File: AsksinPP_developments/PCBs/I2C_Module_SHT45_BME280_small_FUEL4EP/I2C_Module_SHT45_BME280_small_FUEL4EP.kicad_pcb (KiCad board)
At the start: 2 copper layers, 14.1 x 17 mm, 13 parts, among them J1 Conn_01x04, U1 BME280, U2 SHT45-AD1B-R2

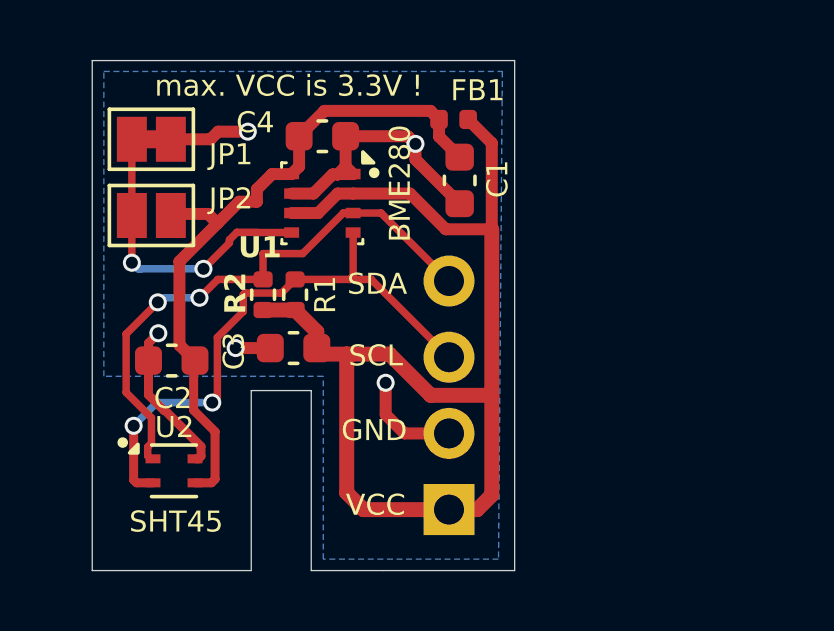
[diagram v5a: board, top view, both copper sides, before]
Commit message: added PCBs/I2C_Module_BME680_small_FUEL4EP; corrected JLCPCB miinimum spacing in DRC rules
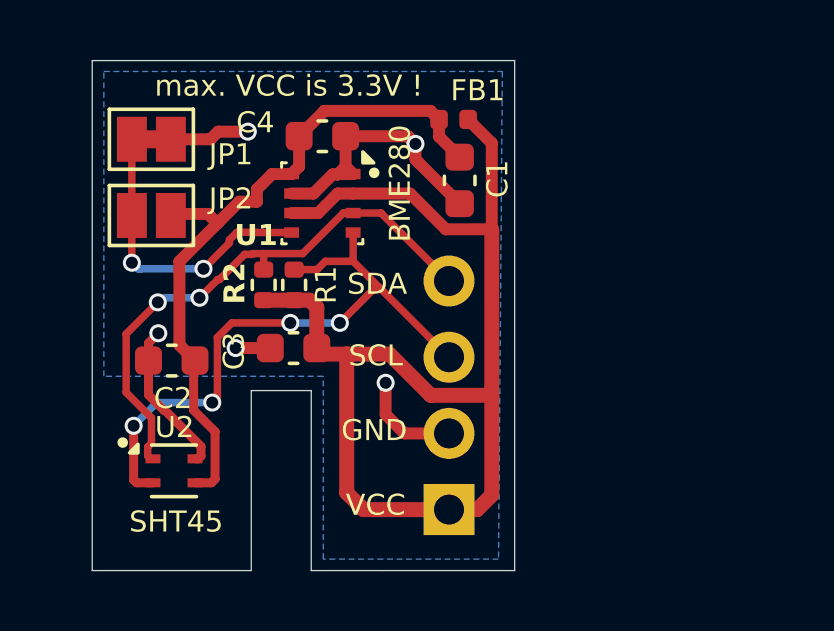
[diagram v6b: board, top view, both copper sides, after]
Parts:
- moved R2 0.33 mm to (6.73, -9.52)
- moved R1 0.33 mm to (5.71, -9.52)
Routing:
- net /SCL: track 19.2 -> 21.3 mm, vias 2 -> 4
- net VCC: track 39.0 -> 39.6 mm
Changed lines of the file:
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@@
 		(tags "lga land grid array")
 		(property "Reference" "U1"
-			(at 1.4732 2.0828 0)
+			(at 1.0668 2.2098 0)
 			(layer "F.SilkS")
 			(effects
@@
 	(footprint "Resistor_SMD:R_0402_1005Metric"
 		(layer "F.Cu")
-		(at 5.6944 -9.1948 -90)
+		(at 5.715 -9.523 -90)
 		(descr "Resistor SMD 0402 (1005 Metric), square (rectangular) end terminal, IPC_7351 nominal, (Body size source: IPC-SM-782 page 72, https://www.pcb-3d.com/wordpress/wp-content/uploads/ipc-sm-782a_amendment_1_and_2.pdf), generated with kicad-footprint-generator")
 		(tags "resistor")
@@
 	(footprint "Resistor_SMD:R_0402_1005Metric"
 		(layer "F.Cu")
-		(at 6.7612 -9.1948 -90)
+		(at 6.731 -9.523 -90)
 		(descr "Resistor SMD 0402 (1005 Metric), square (rectangular) end terminal, IPC_7351 nominal, (Body size source: IPC-SM-782 page 72, https://www.pcb-3d.com/wordpress/wp-content/uploads/ipc-sm-782a_amendment_1_and_2.pdf), generated with kicad-footprint-generator")
 		(tags "resistor")
@@
 	)
 	(segment
-		(start 7.4854 -7.4168)
-		(end 7.4854 -7.9606)
+		(start 6.731 -9.013)
+		(end 5.715 -9.013)
 		(width 0.5)
 		(layer "F.Cu")
@@
 	)
 	(segment
-		(start 7.4854 -7.9606)
-		(end 6.7612 -8.6848)
-		(width 0.5)
+		(start 11.785343 -11.3756)
+		(end 13.318 -11.3756)
+		(width 0.4)
 		(layer "F.Cu")
 		(net 1)
 	)
 	(segment
-		(start 11.785343 -11.3756)
-		(end 13.318 -11.3756)
-		(width 0.4)
+		(start 7.4854 -7.4168)
+		(end 7.4854 -8.7706)
+		(width 0.5)
 		(layer "F.Cu")
 		(net 1)
 	)
 	(segment
-		(start 6.7612 -8.6848)
-		(end 5.6944 -8.6848)
+		(start 7.4854 -8.7706)
+		(end 7.243 -9.013)
 		(width 0.5)
 		(layer "F.Cu")
@@
 	)
 	(segment
+		(start 7.243 -9.013)
+		(end 6.731 -9.013)
+		(width 0.5)
+		(layer "F.Cu")
+		(net 1)
+	)
+	(segment
 		(start 13.2708 -5.842)
 		(end 13.318 -5.7948)
@@
 	)
 	(segment
-		(start 6.3062 -9.2498)
-		(end 6.7612 -9.7048)
-		(width 0.25)
-		(layer "F.Cu")
-		(net 3)
-	)
-	(segment
-		(start 8.6958 -11.2678)
-		(end 8.6958 -9.8134)
-		(width 0.25)
-		(layer "F.Cu")
-		(net 3)
-	)
-	(segment
-		(start 11.892 -7.112)
-		(end 9.3102 -9.6938)
-		(width 0.25)
-		(layer "F.Cu")
-		(net 3)
-	)
-	(segment
-		(start 5.089 -9.2498)
-		(end 6.3062 -9.2498)
+		(start 4.653 -8.255)
+		(end 6.604 -8.255)
 		(width 0.25)
 		(layer "F.Cu")
@@
 	)
 	(segment
-		(start 8.5872 -9.7048)
-		(end 9.2992 -9.7048)
+		(start 7.493 -10.033)
+		(end 6.731 -10.033)
 		(width 0.25)
 		(layer "F.Cu")
@@
 	)
 	(segment
-		(start 5.034 -8.636)
-		(end 5.034 -9.1948)
+		(start 4.17 -7.772)
+		(end 4.653 -8.255)
 		(width 0.25)
 		(layer "F.Cu")
@@
 	)
 	(segment
-		(start 9.2992 -9.7048)
-		(end 9.3102 -9.6938)
+		(start 9.4385 -9.4385)
+		(end 9.5655 -9.4385)
 		(width 0.25)
 		(layer "F.Cu")
@@
 	)
 	(segment
-		(start 8.6958 -9.8134)
-		(end 8.5872 -9.7048)
+		(start 9.5655 -9.4385)
+		(end 8.6958 -10.3082)
 		(width 0.25)
 		(layer "F.Cu")
@@
 	)
 	(segment
-		(start 6.7612 -9.7048)
-		(end 8.5872 -9.7048)
+		(start 8.255 -8.255)
+		(end 9.4385 -9.4385)
 		(width 0.25)
 		(layer "F.Cu")
@@
 	)
 	(segment
-		(start 4.17 -7.772)
-		(end 5.034 -8.636)
+		(start 8.6958 -10.3082)
+		(end 7.7682 -10.3082)
 		(width 0.25)
 		(layer "F.Cu")
@@
 	)
 	(segment
-		(start 5.034 -9.1948)
-		(end 5.089 -9.2498)
+		(start 7.7682 -10.3082)
+		(end 7.493 -10.033)
 		(width 0.25)
 		(layer "F.Cu")
@@
 	)
 	(segment
+		(start 8.6958 -10.3082)
+		(end 8.6958 -11.2678)
+		(width 0.25)
+		(layer "F.Cu")
+		(net 3)
+	)
+	(segment
 		(start 4.17 -7.772)
 		(end 4.17 -5.77)
@@
 		(net 3)
 	)
+	(segment
+		(start 11.892 -7.112)
+		(end 9.5655 -9.4385)
+		(width 0.25)
+		(layer "F.Cu")
+		(net 3)
+	)
+	(via
+		(at 6.604 -8.255)
+		(size 0.6)
+		(drill 0.4)
+		(layers "F.Cu" "B.Cu")
+		(net 3)
+	)
 	(via
 		(at 1.38 -4.826)
@@
 	)
 	(via
+		(at 8.255 -8.255)
+		(size 0.6)
+		(drill 0.4)
+		(layers "F.Cu" "B.Cu")
+		(net 3)
+	)
+	(via
 		(at 4 -5.6)
 		(size 0.6)
@@
 	)
 	(segment
+		(start 6.604 -8.255)
+		(end 8.255 -8.255)
+		(width 0.25)
+		(layer "B.Cu")
+		(net 3)
+	)
+	(segment
 		(start 9.6262 -11.9178)
 		(end 8.6958 -11.9178)
@@
 	)
 	(segment
+		(start 5.6944 -10.5664)
+		(end 5.715 -10.5458)
+		(width 0.25)
+		(layer "F.Cu")
+		(net 4)
+	)
+	(segment
 		(start 11.892 -9.652)
 		(end 9.6262 -11.9178)
@@
 	)
 	(segment
+		(start 5.08 -10.541)
+		(end 5.334 -10.541)
+		(width 0.25)
+		(layer "F.Cu")
+		(net 4)
+	)
+	(segment
 		(start 5.6944 -10.5664)
 		(end 7.0152 -10.5664)
@@
 	)
 	(segment
-		(start 1.85 -3.823222)
-		(end 1.948222 -3.725)
+		(start 5.715 -10.5458)
+		(end 5.715 -10.033)
 		(width 0.25)
 		(layer "F.Cu")
@@
 	)
 	(segment
-		(start 5.6944 -9.7048)
-		(end 4.187592 -9.7048)
+		(start 4.187592 -9.7048)
+		(end 4.2438 -9.7048)
 		(width 0.25)
 		(layer "F.Cu")
@@
 	)
 	(segment
-		(start 1.9745 -5.0915)
-		(end 1.9745 -4.251278)
+		(start 1.85 -3.823222)
+		(end 1.948222 -3.725)
 		(width 0.25)
 		(layer "F.Cu")
@@
 	)
 	(segment
-		(start 5.6944 -9.7048)
-		(end 5.6944 -10.5664)
+		(start 1.9745 -5.0915)
+		(end 1.9745 -4.251278)
 		(width 0.25)
 		(layer "F.Cu")
@@
 	)
 	(segment
+		(start 5.334 -10.541)
+		(end 5.3594 -10.5664)
+		(width 0.25)
+		(layer "F.Cu")
+		(net 4)
+	)
+	(segment
 		(start 8.6958 -11.9178)
 		(end 8.3666 -11.9178)
@@
 	)
 	(segment
+		(start 4.2438 -9.7048)
+		(end 5.08 -10.541)
+		(width 0.25)
+		(layer "F.Cu")
+		(net 4)
+	)
+	(segment
 		(start 1.9745 -4.251278)
 		(end 1.85 -4.126778)
@@
 		(width 0.25)
 		(layer "F.Cu")
+		(net 4)
+	)
+	(segment
+		(start 5.3594 -10.5664)
+		(end 5.6944 -10.5664)
+		(width 0.25)
+		(layer "F.Cu")

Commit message: PCBs: updated some JLCPCB manufacturing data after trial-order
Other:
- board text added: "JLCJLCJLCJLC"
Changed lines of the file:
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@@
 		(sheetfile "I2C_Module_SHT45_BME280_small_FUEL4EP.kicad_sch")
 		(zone_connect 1)
-		(attr exclude_from_pos_files)
+		(attr exclude_from_pos_files exclude_from_bom)
 		(fp_line
 			(start -1.4 -1)
@@
 		(sheetfile "I2C_Module_SHT45_BME280_small_FUEL4EP.kicad_sch")
 		(zone_connect 1)
-		(attr exclude_from_pos_files)
+		(attr exclude_from_pos_files exclude_from_bom)
 		(net_tie_pad_groups "1, 2")
 		(fp_poly
@@
 		(sheetname "Stammblatt")
 		(sheetfile "I2C_Module_SHT45_BME280_small_FUEL4EP.kicad_sch")
-		(attr through_hole exclude_from_pos_files)
+		(attr through_hole exclude_from_pos_files exclude_from_bom)
 		(fp_line
 			(start -1.33 -8.95)
@@
 			(size 1.7 1.7)
 			(drill 1)
-			(layers "*.Cu" "*.Mask")
+			(layers "*.Cu" "*.Mask" "In1.Cu" "In2.Cu" "In3.Cu" "In4.Cu" "In5.Cu" "In6.Cu"
+				"In7.Cu" "In8.Cu" "In9.Cu" "In10.Cu" "In11.Cu" "In12.Cu" "In13.Cu" "In14.Cu"
+				"In15.Cu" "In16.Cu" "In17.Cu" "In18.Cu" "In19.Cu" "In20.Cu" "In21.Cu"
+				"In22.Cu" "In23.Cu" "In24.Cu" "In25.Cu" "In26.Cu" "In27.Cu" "In28.Cu"
+				"In29.Cu" "In30.Cu"
+			)
 			(remove_unused_layers no)
 			(net 1 "VCC")
@@
 			(size 1.7 1.7)
 			(drill 1)
-			(layers "*.Cu" "*.Mask")
+			(layers "*.Cu" "*.Mask" "In1.Cu" "In2.Cu" "In3.Cu" "In4.Cu" "In5.Cu" "In6.Cu"
+				"In7.Cu" "In8.Cu" "In9.Cu" "In10.Cu" "In11.Cu" "In12.Cu" "In13.Cu" "In14.Cu"
+				"In15.Cu" "In16.Cu" "In17.Cu" "In18.Cu" "In19.Cu" "In20.Cu" "In21.Cu"
+				"In22.Cu" "In23.Cu" "In24.Cu" "In25.Cu" "In26.Cu" "In27.Cu" "In28.Cu"
+				"In29.Cu" "In30.Cu"
+			)
 			(remove_unused_layers no)
 			(net 2 "GND")
@@
 			(size 1.7 1.7)
 			(drill 1)
-			(layers "*.Cu" "*.Mask")
+			(layers "*.Cu" "*.Mask" "In1.Cu" "In2.Cu" "In3.Cu" "In4.Cu" "In5.Cu" "In6.Cu"
+				"In7.Cu" "In8.Cu" "In9.Cu" "In10.Cu" "In11.Cu" "In12.Cu" "In13.Cu" "In14.Cu"
+				"In15.Cu" "In16.Cu" "In17.Cu" "In18.Cu" "In19.Cu" "In20.Cu" "In21.Cu"
+				"In22.Cu" "In23.Cu" "In24.Cu" "In25.Cu" "In26.Cu" "In27.Cu" "In28.Cu"
+				"In29.Cu" "In30.Cu"
+			)
 			(remove_unused_layers no)
 			(net 3 "/SCL")
@@
 			(size 1.7 1.7)
 			(drill 1)
-			(layers "*.Cu" "*.Mask")
+			(layers "*.Cu" "*.Mask" "In1.Cu" "In2.Cu" "In3.Cu" "In4.Cu" "In5.Cu" "In6.Cu"
+				"In7.Cu" "In8.Cu" "In9.Cu" "In10.Cu" "In11.Cu" "In12.Cu" "In13.Cu" "In14.Cu"
+				"In15.Cu" "In16.Cu" "In17.Cu" "In18.Cu" "In19.Cu" "In20.Cu" "In21.Cu"
+				"In22.Cu" "In23.Cu" "In24.Cu" "In25.Cu" "In26.Cu" "In27.Cu" "In28.Cu"
+				"In29.Cu" "In30.Cu"
+			)
 			(remove_unused_layers no)
 			(net 4 "/SDA")
@@
 		(sheetname "Stammblatt")
 		(sheetfile "I2C_Module_SHT45_BME280_small_FUEL4EP.kicad_sch")
-		(attr through_hole)
+		(attr through_hole exclude_from_pos_files exclude_from_bom)
 		(fp_poly
 			(pts
@@
 		)
 	)
+	(gr_text "JLCJLCJLCJLC"
+		(at 8.128 -0.889 -90)
+		(layer "B.SilkS")
+		(effects
+			(font
+				(size 0.8128 0.8128)
+				(thickness 0.1524)
+				(bold yes)
+			)
+			(justify left bottom mirror)
+		)
+	)

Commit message: PCB updates
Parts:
- U2: footprint Sensor_Humidity:Sensirion_DFN-4_1.5x1.5mm_P0.8mm_SHT4x_NoCentralPad -> FUEL4EP:Sensirion_DFN-4_1.5x1.5mm_P0.8mm_SHT4x_NoCentralPad
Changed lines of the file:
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@@
+			)
+		)
+		(property "Sim.Enable" ""
+			(at 0 0 -90)
+			(unlocked yes)
+			(layer "F.Fab")
+			(hide yes)
+			(effects
+				(font
+					(size 1 1)
+					(thickness 0.15)
+				)
 			)
 		)
@@
 			)
 		)
+		(property "Sim.Enable" ""
+			(at 0 0 180)
+			(unlocked yes)
+			(layer "F.Fab")
+			(hide yes)
+			(effects
+				(font
+					(size 1 1)
+					(thickness 0.15)
+				)
+			)
+		)
 		(property ki_fp_filters "Inductor_* L_* *Ferrite*")
 		(sheetname "Stammblatt")
@@
 			)
 		)
+		(property "Sim.Enable" ""
+			(at 0 0 0)
+			(unlocked yes)
+			(layer "F.Fab")
+			(hide yes)
+			(effects
+				(font
+					(size 1 1)
+					(thickness 0.15)
+				)
+			)
+		)
 		(property ki_fp_filters "SolderJumper*Open*")
 		(sheetname "Stammblatt")
@@
 			)
 		)
+		(property "Sim.Enable" ""
+			(at 0 0 -90)
+			(unlocked yes)
+			(layer "F.Fab")
+			(hide yes)
+			(effects
+				(font
+					(size 1 1)
+					(thickness 0.15)
+				)
+			)
+		)
 		(property ki_fp_filters "*LGA*2.5x2.5mm*P0.65mm*Clockwise*")
 		(sheetname "Stammblatt")
@@
 				(font
 					(size 1.27 1.27)
+					(thickness 0.15)
+				)
+			)
+		)
+		(property "Sim.Enable" ""
+			(at 0 0 180)
+			(unlocked yes)
+			(layer "F.Fab")
+			(hide yes)
+			(effects
+				(font
+					(size 1 1)
 					(thickness 0.15)
 				)
@@
 			)
 		)
+		(property "Sim.Enable" ""
+			(at 0 0 0)
+			(unlocked yes)
+			(layer "F.Fab")
+			(hide yes)
+			(effects
+				(font
+					(size 1 1)
+					(thickness 0.15)
+				)
+			)
+		)
 		(property ki_fp_filters "C_*")
 		(sheetname "Stammblatt")
@@
 			)
 		)
+		(property "Sim.Enable" ""
+			(at 0 0 -90)
+			(unlocked yes)
+			(layer "F.Fab")
+			(hide yes)
+			(effects
+				(font
+					(size 1 1)
+					(thickness 0.15)
+				)
+			)
+		)
 		(property ki_fp_filters "R_*")
 		(sheetname "Stammblatt")
@@
 		)
 	)
-	(footprint "Sensor_Humidity:Sensirion_DFN-4_1.5x1.5mm_P0.8mm_SHT4x_NoCentralPad"
+	(footprint "FUEL4EP:Sensirion_DFN-4_1.5x1.5mm_P0.8mm_SHT4x_NoCentralPad"
 		(layer "F.Cu")
 		(at 2.725 -3.325)
@@
 		(tags "DFN NoLead")
 		(property "Reference" "U2"
-			(at 0.0182 -1.4502 0)
-			(layer "F.SilkS")
-			(effects
-				(font
-					(size 0.7 0.7)
+			(at 0 -1.7 0)
+			(layer "F.SilkS")
+			(hide yes)
+			(effects
+				(font
+					(size 1 1)
 					(thickness 0.15)
 				)
@@
 			(at 0 1.7 0)
 			(layer "F.Fab")
-			(effects
-				(font
-					(size 1 1)
-					(thickness 0.15)
-				)
-			)
-		)
-		(property "Footprint" "Sensor_Humidity:Sensirion_DFN-4_1.5x1.5mm_P0.8mm_SHT4x_NoCentralPad"
+			(hide yes)
+			(effects
+				(font
+					(size 1 1)
+					(thickness 0.15)
+				)
+			)
+		)
+		(property "Footprint" "FUEL4EP:Sensirion_DFN-4_1.5x1.5mm_P0.8mm_SHT4x_NoCentralPad"
 			(at 0 0 0)
 			(unlocked yes)
@@
 			)
 		)
-		(property "Description" "Digital Humidity and Temperature Sensor, +/-1%RH, +/-0.1degC, I2C, 1.08-3.6V, 16bit, DFN-4"
+		(property "Description" "Digital Humidity and Temperature Sensor, ±1%RH, ±0.1°C, I2C, 1.08-3.6V, 16bit, DFN-4"
 			(at 0 0 0)
 			(unlocked yes)
@@
 		)
 		(property "TYPE" "DFN-4"
+			(at 0 0 0)
+			(unlocked yes)
+			(layer "F.Fab")
+			(hide yes)
+			(effects
+				(font
+					(size 1 1)
+					(thickness 0.15)
+				)
+			)
+		)
+		(property "Sim.Enable" ""
 			(at 0 0 0)
 			(unlocked yes)
@@
 			)
 		)
-		(model "${KICAD8_3DMODEL_DIR}/Sensor_Humidity.3dshapes/Sensirion_DFN-4_1.5x1.5mm_P0.8mm_SHT4x_NoCentralPad.wrl"
+		(model "/home/ewald/CAD/git/HomeAutomation/AsksinPP_developments/PCBs/FUEL4EP_kicad_3D_models/SHT45-AD1F-R2.step"
 			(offset
 				(xyz 0 0 0)
@@
 			)
 			(rotate
-				(xyz 0 0 0)
+				(xyz -90 0 0)
 			)
 		)
@@
 			)
 		)
+		(property "Sim.Enable" ""
+			(at 0 0 180)
+			(unlocked yes)
+			(layer "F.Fab")
+			(hide yes)
+			(effects
+				(font
+					(size 1 1)
+					(thickness 0.15)
+				)
+			)
+		)
 		(property ki_fp_filters "C_*")
 		(sheetname "Stammblatt")
@@
 			)
 		)
+		(property "Sim.Enable" ""
+			(at 0 0 -90)
+			(unlocked yes)
+			(layer "F.Fab")
+			(hide yes)
+			(effects
+				(font
+					(size 1 1)
+					(thickness 0.15)
+				)
+			)
+		)
 		(property ki_fp_filters "R_*")
 		(sheetname "Stammblatt")
@@
 		(property "TYPE" "0603"
 			(at 0 0 0)
+			(layer "F.Fab")
+			(hide yes)
+			(effects
+				(font
+					(size 1 1)
+					(thickness 0.15)
+				)
+			)
+		)
+		(property "Sim.Enable" ""
+			(at 0 0 0)
+			(unlocked yes)
 			(layer "F.Fab")
 			(hide yes)
@@
 			)
 		)
+		(property "Sim.Enable" ""
+			(at 0 0 0)
+			(unlocked yes)
+			(layer "B.Fab")
+			(hide yes)
+			(effects
+				(font
+					(size 1 1)
+					(thickness 0.15)
+				)
+				(justify mirror)
+			)
+		)
 		(property ki_fp_filters "Connector*:*_1x??_*")
 		(sheetname "Stammblatt")
 		(sheetfile "I2C_Module_SHT45_BME280_small_FUEL4EP.kicad_sch")
-		(attr through_hole exclude_from_pos_files exclude_from_bom)
+		(attr through_hole exclude_from_pos_files)
 		(fp_line
 			(start -1.33 -8.95)
@@
 			)
 		)
-		(property "Sim.Enable" "0"
+		(property "Sim.Enable" ""
 			(at 11.0284 -5.3292 0)
 			(layer "B.Fab")
@@
 		(sheetname "Stammblatt")
 		(sheetfile "I2C_Module_SHT45_BME280_small_FUEL4EP.kicad_sch")
-		(attr through_hole exclude_from_pos_files exclude_from_bom)
+		(attr through_hole exclude_from_pos_files)
 		(fp_poly
 			(pts
